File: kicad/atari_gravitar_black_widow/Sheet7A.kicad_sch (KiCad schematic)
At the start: 28 parts

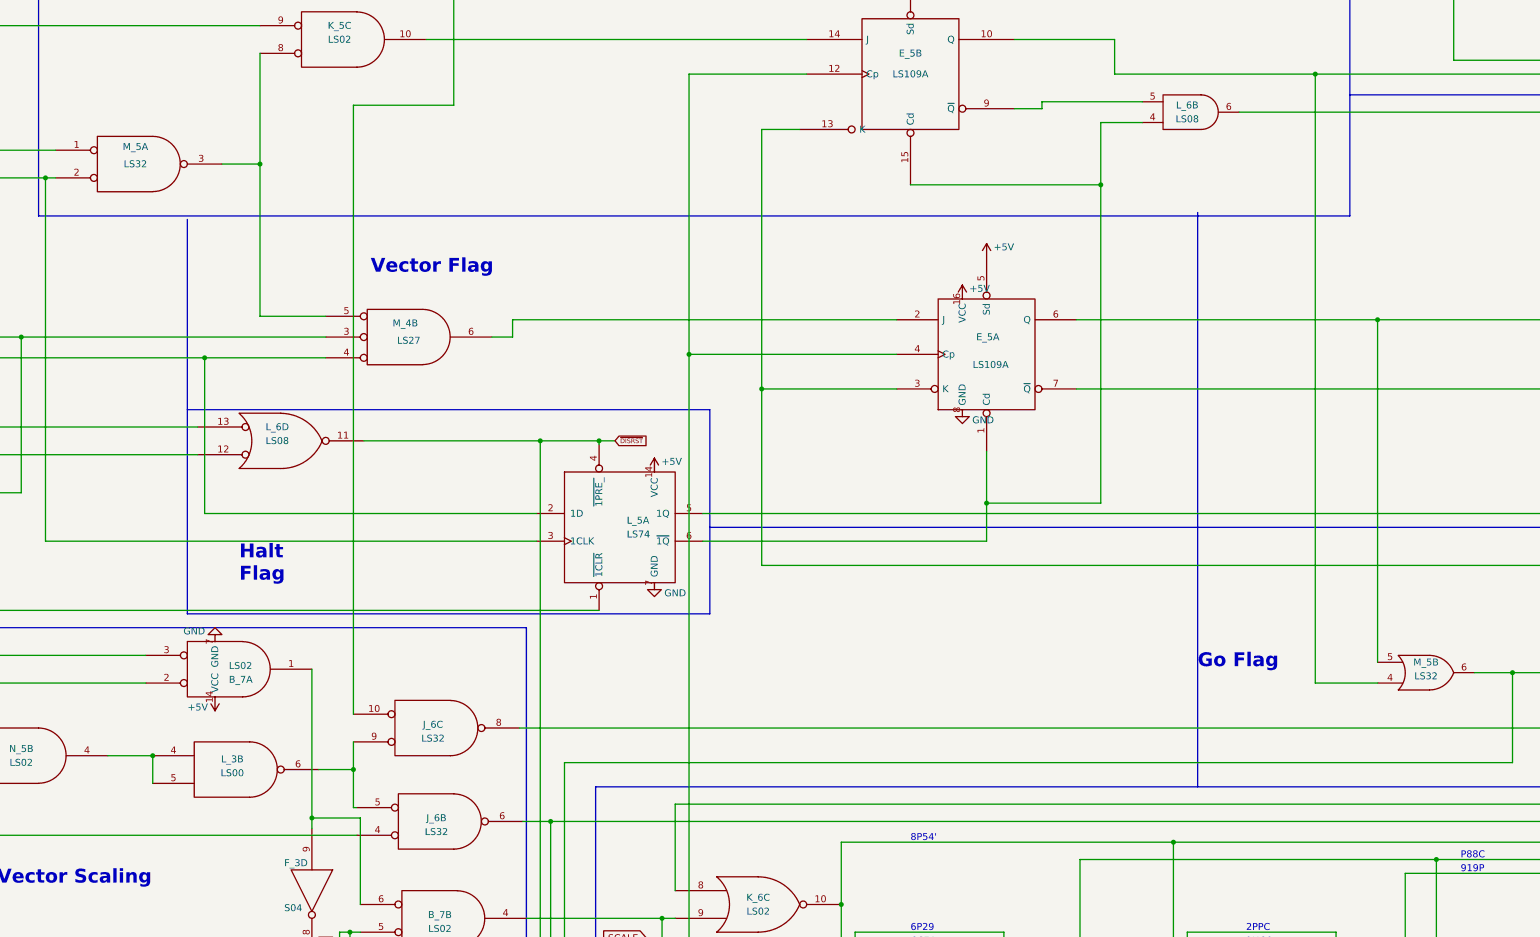
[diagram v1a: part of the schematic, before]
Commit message: Fixed all schematic warnings and fixed the edge cuts
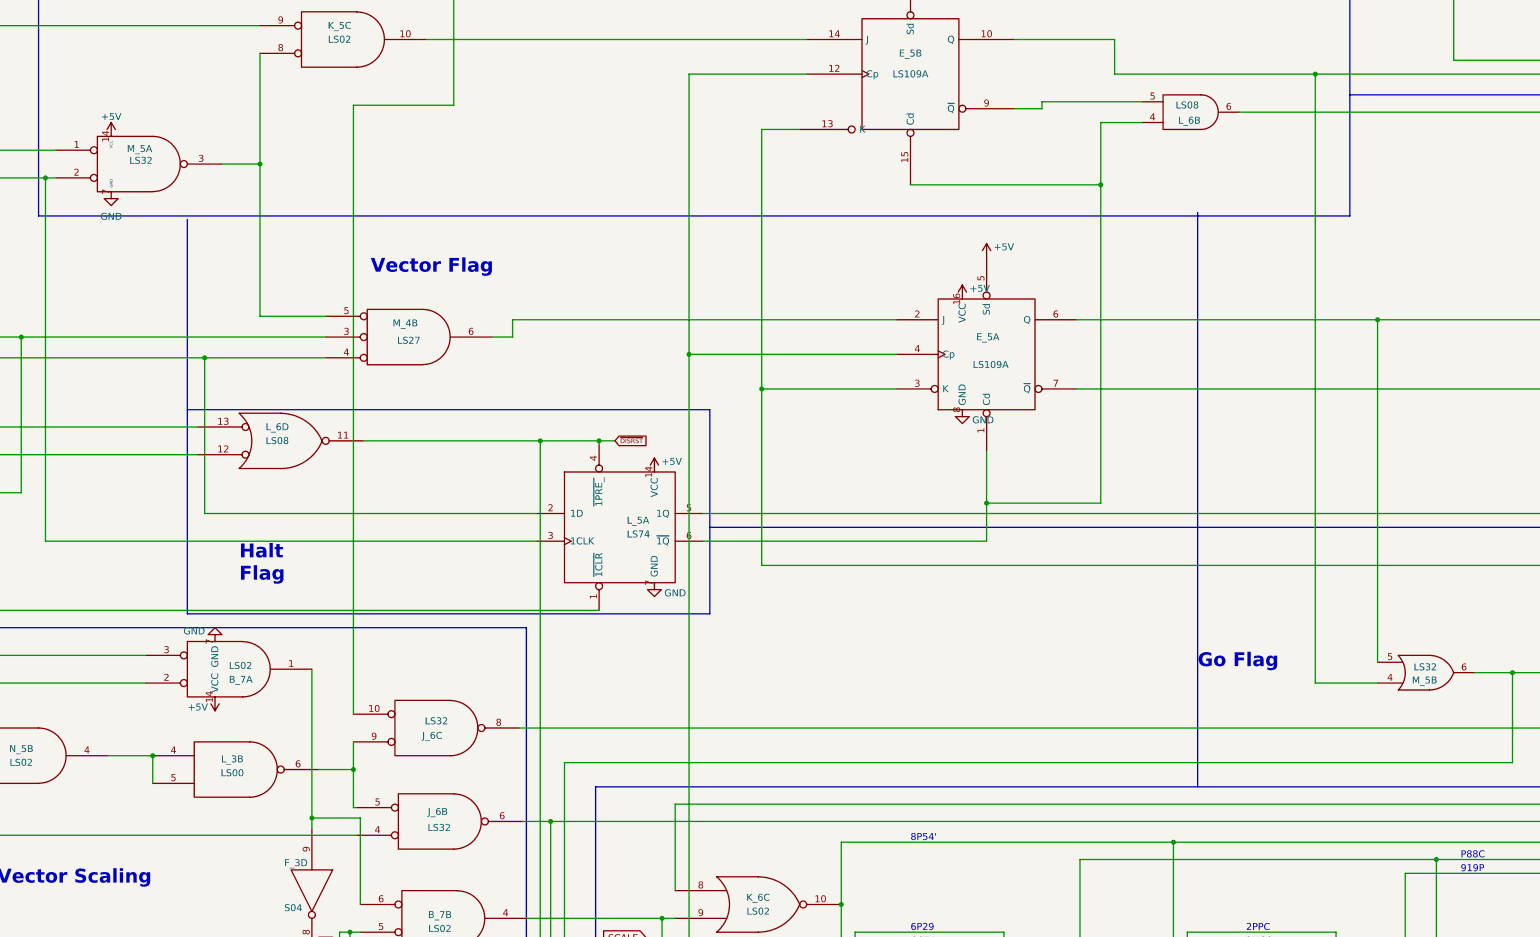
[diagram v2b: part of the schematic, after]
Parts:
- removed J_6, M_5: LS32, Star_Wars_Vector_PCB:DIP14, symbol atari_grav_bw:LS32
- removed unit 2 of L_6
- added J_6, M_5: LS32, Star_Wars_Vector_PCB:DIP14, symbol Star_Wars_Vector_PCB:LS32
- added unit 2 of L_6
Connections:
- net GO: now also M_5.6
- net VCTR: now also M_5.5
- net ~{CENTER}: now also L_6.6
- net at E_5.10 (Q), J_5.9: now also M_5.4
- net at E_5.1 (Cd), E_5.15 (Cd), L_5.6 (~{1Q}): now also L_6.4
- net at E_5.9 (~{Q}): now also L_6.5
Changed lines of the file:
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@@
-    (pin "6")
-  )
-  (symbol (lib_id "Star_Wars_Vector_PCB:LS08") (at 275.59 121.92 0) (mirror x) (unit 2)
-    (in_bom yes) (on_board yes)
-    (property "Reference" "L_6" (id 0) (at 275.59 120.65 0))
-    (property "Value" "LS08" (id 1) (at 275.59 123.19 0))
-    (property "Footprint" "Star_Wars_Vector_PCB:DIP14" (id 2) (at 275.59 121.92 0)
-      (effects (font (size 1.27 1.27)) hide)
-    )
-    (property "Datasheet" "" (id 3) (at 275.59 121.92 0)
-      (effects (font (size 1.27 1.27)) hide)
-    )
-    (pin "4")
-    (pin "5")
     (pin "6")
   )
@@
     (pin "6")
     (pin "7")
-  )
-  (symbol (lib_id "atari_grav_bw:LS32") (at 319.405 224.79 0) (mirror x) (unit 2)
-    (in_bom yes) (on_board yes)
-    (property "Reference" "M_5" (id 0) (at 319.405 222.885 0))
-    (property "Value" "LS32" (id 1) (at 319.405 225.425 0))
-    (property "Footprint" "Star_Wars_Vector_PCB:DIP14" (id 2) (at 319.405 224.79 0)
-      (effects (font (size 1.27 1.27)) hide)
-    )
-    (property "Datasheet" "" (id 3) (at 319.405 224.79 0)
-      (effects (font (size 1.27 1.27)) hide)
-    )
-    (pin "4")
-    (pin "5")
-    (pin "6")
   )
   (symbol (lib_id "Star_Wars_Vector_PCB:LS86") (at 329.565 69.85 0) (unit 2)
@@
     (pin "9")
   )
-  (symbol (lib_id "atari_grav_bw:LS32") (at 83.185 131.445 0) (unit 1) (convert 2)
-    (in_bom yes) (on_board yes)
-    (property "Reference" "M_5" (id 0) (at 82.55 128.27 0))
-    (property "Value" "LS32" (id 1) (at 82.55 131.445 0))
-    (property "Footprint" "Star_Wars_Vector_PCB:DIP14" (id 2) (at 83.185 131.445 0)
-      (effects (font (size 1.27 1.27)) hide)
-    )
-    (property "Datasheet" "" (id 3) (at 83.185 131.445 0)
-      (effects (font (size 1.27 1.27)) hide)
-    )
-    (pin "1")
-    (pin "2")
-    (pin "3")
-  )
   (symbol (lib_id "atari_grav_bw:LS02") (at 120.65 108.585 0) (mirror x) (unit 3) (convert 2)
     (in_bom yes) (on_board yes)
@@
     (pin "5")
     (pin "6")
-  )
-  (symbol (lib_id "atari_grav_bw:LS32") (at 138.43 252.095 0) (mirror x) (unit 2) (convert 2)
-    (in_bom yes) (on_board yes)
-    (property "Reference" "J_6" (id 0) (at 137.795 251.46 0))
-    (property "Value" "LS32" (id 1) (at 137.795 254 0))
-    (property "Footprint" "Star_Wars_Vector_PCB:DIP14" (id 2) (at 138.43 252.095 0)
-      (effects (font (size 1.27 1.27)) hide)
-    )
-    (property "Datasheet" "" (id 3) (at 138.43 252.095 0)
-      (effects (font (size 1.27 1.27)) hide)
-    )
-    (pin "4")
-    (pin "5")
-    (pin "6")
-  )
-  (symbol (lib_id "atari_grav_bw:LS32") (at 137.795 234.95 0) (mirror x) (unit 3) (convert 2)
-    (in_bom yes) (on_board yes)
-    (property "Reference" "J_6" (id 0) (at 137.16 234.315 0))
-    (property "Value" "LS32" (id 1) (at 137.16 236.855 0))
-    (property "Footprint" "Star_Wars_Vector_PCB:DIP14" (id 2) (at 137.795 234.95 0)
-      (effects (font (size 1.27 1.27)) hide)
-    )
-    (property "Datasheet" "" (id 3) (at 137.795 234.95 0)
-      (effects (font (size 1.27 1.27)) hide)
-    )
-    (pin "10")
-    (pin "8")
-    (pin "9")
   )
   (symbol (lib_id "atari_grav_bw:LS00") (at 100.965 242.57 0) (unit 2)
@@
     (pin "1")
   )
+  (symbol (lib_id "Star_Wars_Vector_PCB:LS32") (at 138.43 252.095 0) (mirror x) (unit 2) (convert 2)
+    (in_bom yes) (on_board yes)
+    (property "Reference" "J_6" (id 0) (at 138.049 250.317 0))
+    (property "Value" "LS32" (id 1) (at 138.303 253.238 0))
+    (property "Footprint" "Star_Wars_Vector_PCB:DIP14" (id 2) (at 138.43 252.095 0)
+      (effects (font (size 1.27 1.27)) hide)
+    )
+    (property "Datasheet" "" (id 3) (at 138.43 252.095 0)
+      (effects (font (size 1.27 1.27)) hide)
+    )
+    (pin "4")
+    (pin "5")
+    (pin "6")
+  )
   (symbol (lib_id "power:+5V") (at 97.155 229.235 180) (unit 1)
     (in_bom yes) (on_board yes)
@@
     (pin "1")
   )
+  (symbol (lib_id "Star_Wars_Vector_PCB:LS32") (at 319.405 224.79 0) (mirror x) (unit 2)
+    (in_bom yes) (on_board yes)
+    (property "Reference" "M_5" (id 0) (at 319.151 226.187 0))
+    (property "Value" "LS32" (id 1) (at 319.278 223.774 0))
+    (property "Footprint" "Star_Wars_Vector_PCB:DIP14" (id 2) (at 319.405 224.79 0)
+      (effects (font (size 1.27 1.27)) hide)
+    )
+    (property "Datasheet" "" (id 3) (at 319.405 224.79 0)
+      (effects (font (size 1.27 1.27)) hide)
+    )
+    (pin "4")
+    (pin "5")
+    (pin "6")
+  )
   (symbol (lib_id "power:+5V") (at 238.76 148.59 0) (unit 1)
     (in_bom yes) (on_board yes)
@@
     )
     (property "Datasheet" "" (id 3) (at 238.76 148.59 0)
+      (effects (font (size 1.27 1.27)) hide)
+    )
+    (pin "1")
+  )
+  (symbol (lib_id "Star_Wars_Vector_PCB:LS32") (at 137.795 234.95 0) (mirror x) (unit 3) (convert 2)
+    (in_bom yes) (on_board yes)
+    (property "Reference" "J_6" (id 0) (at 137.033 236.347 0))
+    (property "Value" "LS32" (id 1) (at 137.795 233.68 0))
+    (property "Footprint" "Star_Wars_Vector_PCB:DIP14" (id 2) (at 137.795 234.95 0)
+      (effects (font (size 1.27 1.27)) hide)
+    )
+    (property "Datasheet" "" (id 3) (at 137.795 234.95 0)
+      (effects (font (size 1.27 1.27)) hide)
+    )
+    (pin "10")
+    (pin "8")
+    (pin "9")
+  )
+  (symbol (lib_id "power:GND") (at 78.105 136.525 0) (unit 1)
+    (in_bom yes) (on_board yes) (fields_autoplaced)
+    (property "Reference" "#PWR0317" (id 0) (at 78.105 142.875 0)
+      (effects (font (size 1.27 1.27)) hide)
+    )
+    (property "Value" "GND" (id 1) (at 78.105 141.0875 0))
+    (property "Footprint" "" (id 2) (at 78.105 136.525 0)
+      (effects (font (size 1.27 1.27)) hide)
+    )
+    (property "Datasheet" "" (id 3) (at 78.105 136.525 0)
       (effects (font (size 1.27 1.27)) hide)
     )
@@
     (pin "9")
   )
+  (symbol (lib_id "power:+5V") (at 78.105 126.365 0) (unit 1)
+    (in_bom yes) (on_board yes) (fields_autoplaced)
+    (property "Reference" "#PWR0318" (id 0) (at 78.105 130.175 0)
+      (effects (font (size 1.27 1.27)) hide)
+    )
+    (property "Value" "+5V" (id 1) (at 78.105 122.7605 0))
+    (property "Footprint" "" (id 2) (at 78.105 126.365 0)
+      (effects (font (size 1.27 1.27)) hide)
+    )
+    (property "Datasheet" "" (id 3) (at 78.105 126.365 0)
+      (effects (font (size 1.27 1.27)) hide)
+    )
+    (pin "1")
+  )
   (symbol (lib_id "power:+5V") (at 234.315 156.21 0) (unit 1)
     (in_bom yes) (on_board yes)
@@
     (pin "2")
   )
+  (symbol (lib_id "Star_Wars_Vector_PCB:LS32") (at 83.185 131.445 0) (unit 1) (convert 2)
+    (in_bom yes) (on_board yes)
+    (property "Reference" "M_5" (id 0) (at 83.312 128.651 0))
+    (property "Value" "LS32" (id 1) (at 83.566 130.81 0))
+    (property "Footprint" "Star_Wars_Vector_PCB:DIP14" (id 2) (at 83.185 131.445 0)
+      (effects (font (size 1.27 1.27)) hide)
+    )
+    (property "Datasheet" "" (id 3) (at 83.185 131.445 0)
+      (effects (font (size 1.27 1.27)) hide)
+    )
+    (pin "1")
+    (pin "14")
+    (pin "2")
+    (pin "3")
+    (pin "7")
+  )
   (symbol (lib_id "atari_grav_bw:TP") (at 518.287 181.483 0) (unit 1)
     (in_bom yes) (on_board yes)
@@
     (pin "2")
   )
+  (symbol (lib_id "atari_grav_bw:LS08") (at 275.59 121.92 0) (mirror x) (unit 2)
+    (in_bom yes) (on_board yes)
+    (property "Reference" "L_6" (id 0) (at 275.971 123.444 0))
+    (property "Value" "LS08" (id 1) (at 275.59 120.65 0))
+    (property "Footprint" "Star_Wars_Vector_PCB:DIP14" (id 2) (at 275.59 121.92 0)
+      (effects (font (size 1.27 1.27)) hide)
+    )
+    (property "Datasheet" "" (id 3) (at 275.59 121.92 0)
+      (effects (font (size 1.27 1.27)) hide)
+    )
+    (pin "4")
+    (pin "5")
+    (pin "6")
+  )
 )

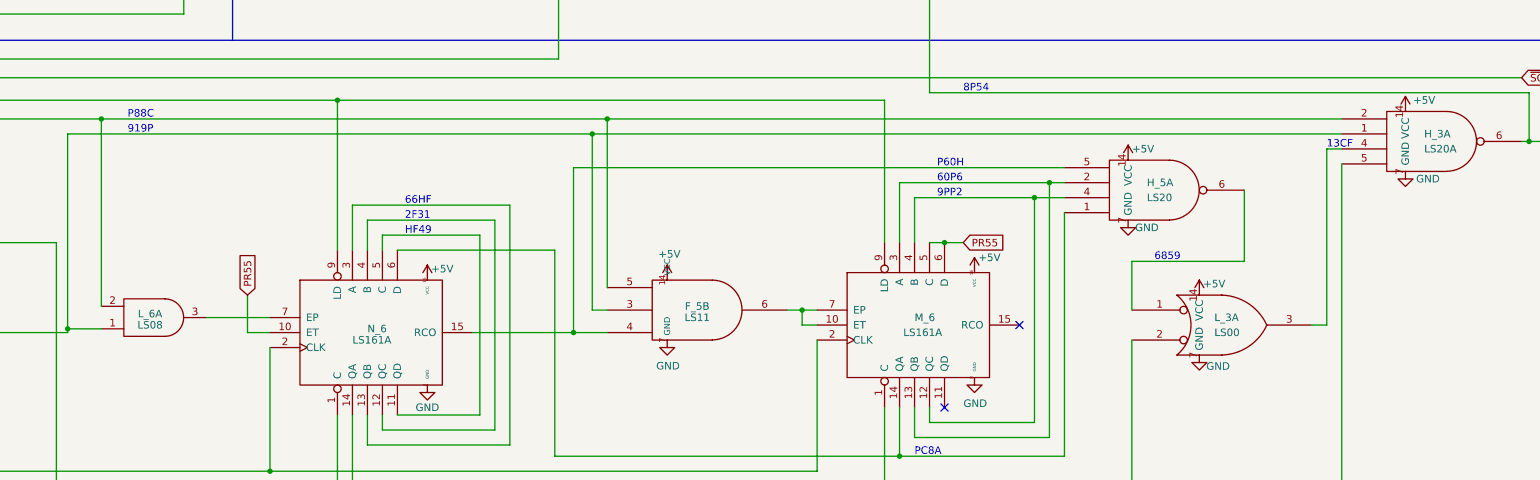
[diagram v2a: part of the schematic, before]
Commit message: Fixed all warning on PCB layout
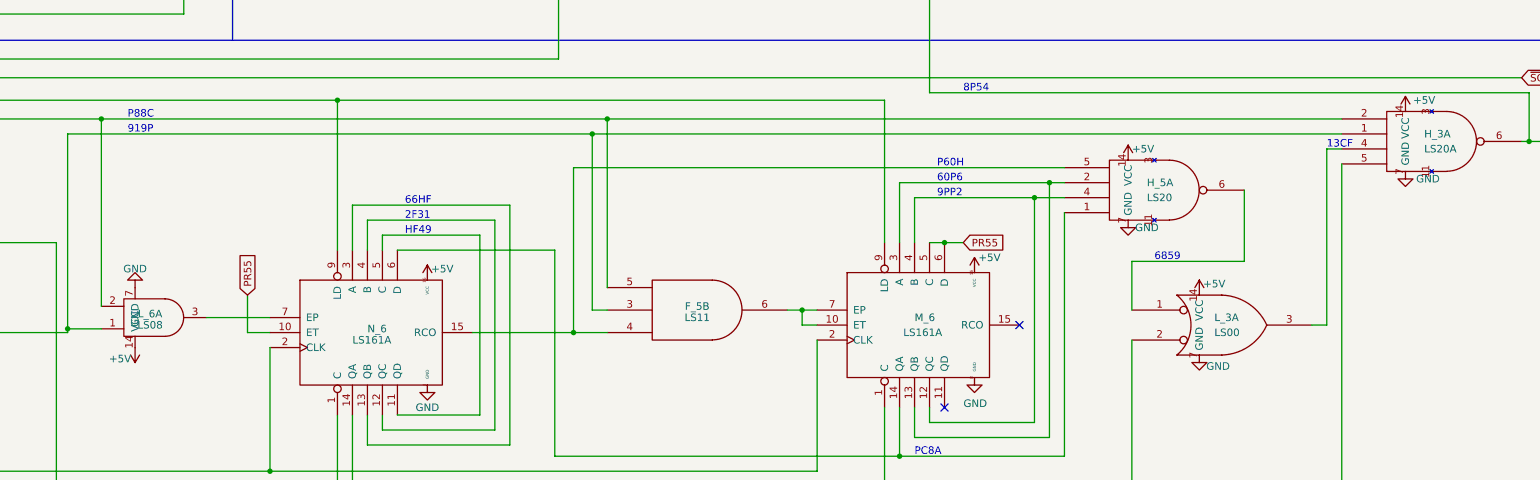
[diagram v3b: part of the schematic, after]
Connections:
- net +5V: now also L_6.14 (VCC); no longer F_5.14 (VCC)
- net GND: now also L_6.7 (GND); no longer F_5.7 (GND)
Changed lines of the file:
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@@
     )
     (pin "1")
-    (pin "2")
-    (pin "3")
+    (pin "14")
+    (pin "2")
+    (pin "3")
+    (pin "7")
   )
   (symbol (lib_id "atari_grav_bw:LS161A") (at 218.44 295.275 0) (unit 1)
@@
       (effects (font (size 1.27 1.27)) hide)
     )
-    (pin "14")
-    (pin "7")
     (pin "3")
     (pin "4")
@@
     (pin "1")
   )
-  (symbol (lib_id "power:GND") (at 417.195 296.545 0) (unit 1)
-    (in_bom yes) (on_board yes)
-    (property "Reference" "#PWR0200" (id 0) (at 417.195 302.895 0)
-      (effects (font (size 1.27 1.27)) hide)
-    )
-    (property "Value" "GND" (id 1) (at 417.322 300.9392 0))
-    (property "Footprint" "" (id 2) (at 417.195 296.545 0)
-      (effects (font (size 1.27 1.27)) hide)
-    )
-    (property "Datasheet" "" (id 3) (at 417.195 296.545 0)
-      (effects (font (size 1.27 1.27)) hide)
-    )
-    (pin "1")
-  )
   (symbol (lib_id "power:GND") (at 376.555 304.165 0) (unit 1)
     (in_bom yes) (on_board yes)
@@
     )
     (property "Datasheet" "" (id 3) (at 376.555 286.385 0)
-      (effects (font (size 1.27 1.27)) hide)
-    )
-    (pin "1")
-  )
-  (symbol (lib_id "power:+5V") (at 417.195 286.385 0) (unit 1)
-    (in_bom yes) (on_board yes)
-    (property "Reference" "#PWR0195" (id 0) (at 417.195 290.195 0)
-      (effects (font (size 1.27 1.27)) hide)
-    )
-    (property "Value" "+5V" (id 1) (at 417.576 281.9908 0))
-    (property "Footprint" "" (id 2) (at 417.195 286.385 0)
-      (effects (font (size 1.27 1.27)) hide)
-    )
-    (property "Datasheet" "" (id 3) (at 417.195 286.385 0)
       (effects (font (size 1.27 1.27)) hide)
     )
@@
     (pin "7")
     (pin "1")
-    (pin "2")
+    (pin "11")
+    (pin "2")
+    (pin "3")
     (pin "4")
     (pin "5")
@@
     )
     (pin "1")
-    (pin "14")
-    (pin "2")
+    (pin "11")
+    (pin "14")
+    (pin "2")
+    (pin "3")
     (pin "4")
     (pin "5")
@@
     )
     (property "Datasheet" "" (id 3) (at 542.29 257.81 0)
+      (effects (font (size 1.27 1.27)) hide)
+    )
+    (pin "1")
+  )
+  (symbol (lib_id "power:GND") (at 327.025 287.655 180) (unit 1)
+    (in_bom yes) (on_board yes)
+    (property "Reference" "#PWR0556" (id 0) (at 327.025 281.305 0)
+      (effects (font (size 1.27 1.27)) hide)
+    )
+    (property "Value" "GND" (id 1) (at 327.025 284.48 0))
+    (property "Footprint" "" (id 2) (at 327.025 287.655 0)
+      (effects (font (size 1.27 1.27)) hide)
+    )
+    (property "Datasheet" "" (id 3) (at 327.025 287.655 0)
       (effects (font (size 1.27 1.27)) hide)
     )
@@
       (effects (font (size 1.27 1.27)) hide)
     )
+    (pin "1")
+  )
+  (symbol (lib_id "power:+5V") (at 327.025 297.815 180) (unit 1)
+    (in_bom yes) (on_board yes)
+    (property "Reference" "#PWR0555" (id 0) (at 327.025 294.005 0)
+      (effects (font (size 1.27 1.27)) hide)
+    )
+    (property "Value" "+5V" (id 1) (at 324.485 299.72 0))
+    (property "Footprint" "" (id 2) (at 327.025 297.815 0)
+      (effects (font (size 1.27 1.27)) hide)
+    )
+    (property "Datasheet" "" (id 3) (at 327.025 297.815 0)
+      (effects (font (size 1.27 1.27)) hide)
+    )

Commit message: traces and more traces
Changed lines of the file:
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@@
   (junction (at 66.04 133.985) (diameter 0) (color 0 0 0 0)
   )
+  (junction (at 139.45 67.31) (diameter 0) (color 0 0 0 0)
+  )
   (junction (at 212.09 267.335) (diameter 0) (color 0 0 0 0)
   )
@@
   )
   (junction (at 184.15 166.37) (diameter 0) (color 0 0 0 0)
-  )
-  (junction (at 140.97 80.01) (diameter 0) (color 0 0 0 0)
   )
   (junction (at 167.64 182.245) (diameter 0) (color 0 0 0 0)
@@
     (stroke (width 0) (type default) (color 0 0 0 0))
   )
+  (wire (pts (xy 139.45 67.31) (xy 50.165 67.31))
+    (stroke (width 0) (type default) (color 0 0 0 0))
+  )
   (wire (pts (xy 495.935 283.21) (xy 495.935 291.465))
     (stroke (width 0) (type default) (color 0 0 0 0))
@@
     (stroke (width 0) (type default) (color 0 0 0 0))
   )
-  (wire (pts (xy 140.97 120.65) (xy 140.97 80.01))
+  (wire (pts (xy 139.45 107.95) (xy 139.45 67.31))
     (stroke (width 0) (type default) (color 0 0 0 0))
   )
@@
     (stroke (width 0) (type default) (color 0 0 0 0))
   )
-  (wire (pts (xy 122.555 120.65) (xy 140.97 120.65))
+  (wire (pts (xy 122.555 120.65) (xy 139.45 107.95))
     (stroke (width 0) (type default) (color 0 0 0 0))
   )
@@
     (stroke (width 0) (type default) (color 0 0 0 0))
   )
-  (wire (pts (xy 314.325 67.31) (xy 50.165 67.31))
+  (wire (pts (xy 314.325 67.31) (xy 139.45 67.31))
     (stroke (width 0) (type default) (color 0 0 0 0))
   )
@@
     (stroke (width 0) (type default) (color 0 0 0 0))
   )
-  (wire (pts (xy 140.97 80.01) (xy 50.165 80.01))
+  (wire (pts (xy 50.165 80.01) (xy 314.325 80.01))
     (stroke (width 0) (type default) (color 0 0 0 0))
   )
@@
     (stroke (width 0) (type default) (color 0 0 0 0))
   )
-  (wire (pts (xy 314.325 80.01) (xy 140.97 80.01))
-    (stroke (width 0) (type default) (color 0 0 0 0))
-  )
